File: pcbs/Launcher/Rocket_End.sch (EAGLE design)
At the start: 28 parts, among them IC1 7805TV, K4 LD105, K5 LD105, K6 LD105, K7 LD105, T1 BC547, T2 BC547, T3 BC547, T4 BC547, T5 BC547, U1 ARDUINO-MEGAPRO-5V, X1 22-23-2041, X2 22-23-2041, X4 22-23-2021, X5 22-23-2021, X6 22-23-2021

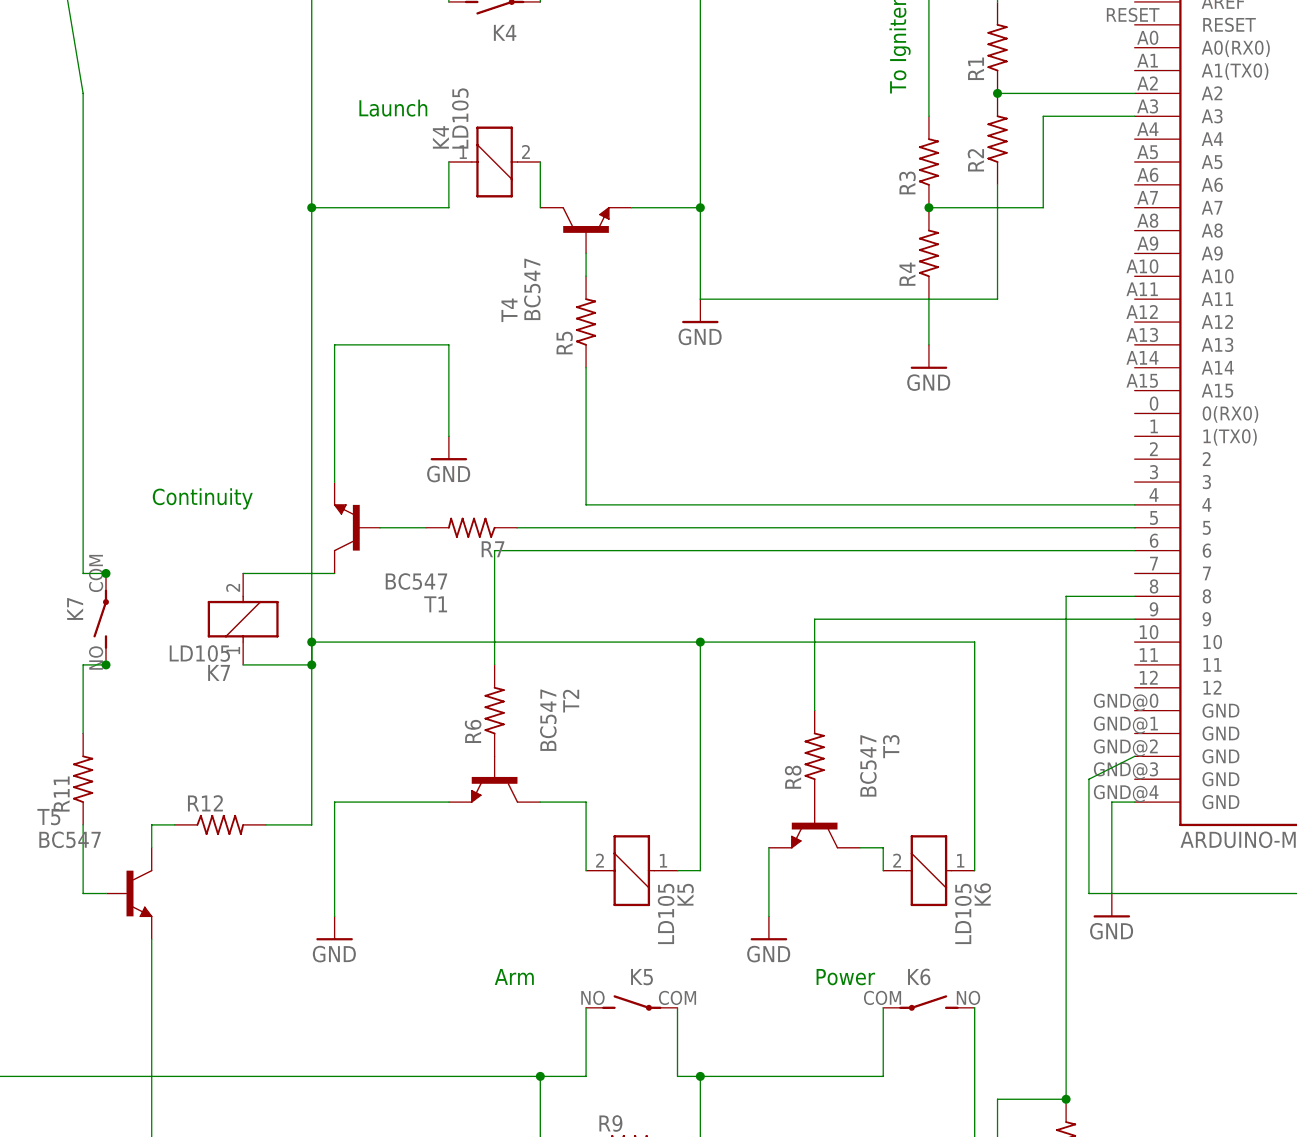
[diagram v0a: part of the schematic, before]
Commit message: * Much better placement of components and tracks for Rocket_End * Put IMU on bottom of the Sensor board
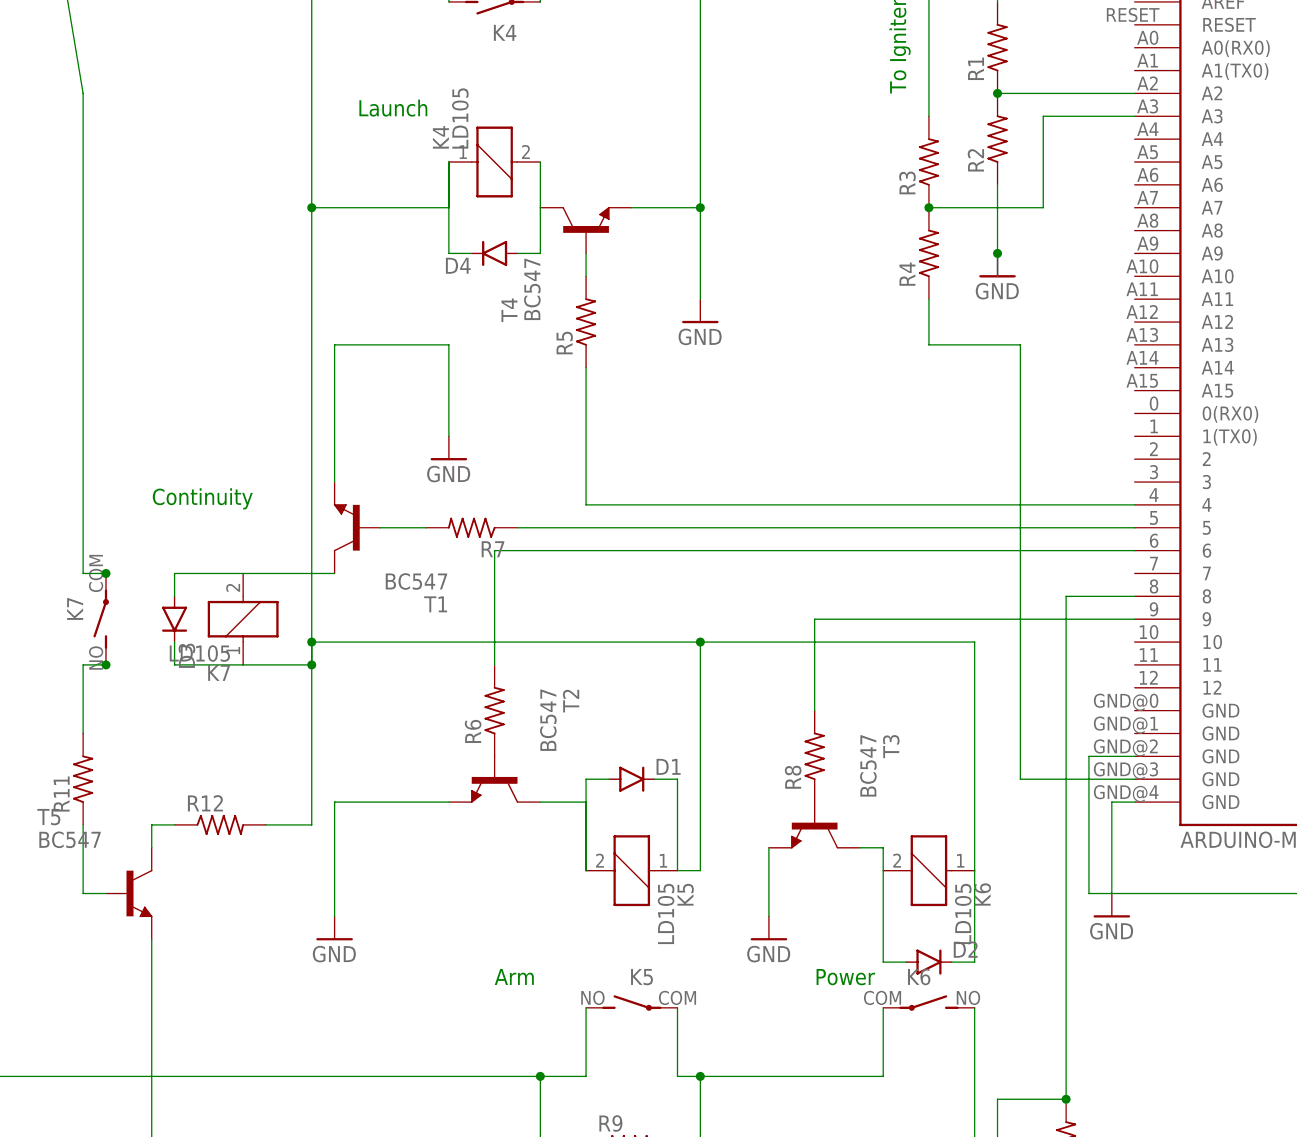
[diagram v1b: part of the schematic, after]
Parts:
- added D1, D2, D3, D4: (no value), SparkFun-DiscreteSemi:DIODE1N4148
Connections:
- new net N$24: R4.1, U1.GND@3
- net GND: no longer R4.1
- net N$19: now also D4.A
- net N$20: now also D3.A
- net N$21: now also D2.A
- net N$22: now also D1.A
- net N$5: now also D1.C, D2.C, D3.C, D4.C
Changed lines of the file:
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@@
 <?xml version="1.0" encoding="utf-8"?>
 <!DOCTYPE eagle SYSTEM "eagle.dtd">
-<eagle version="7.3.0">
+<eagle version="7.1.0">
 <drawing>
 <settings>
@@
 <layer number="223" name="223bmp" color="24" fill="1" visible="no" active="no"/>
 <layer number="224" name="224bmp" color="25" fill="1" visible="no" active="no"/>
+<layer number="225" name="225bmp" color="7" fill="1" visible="yes" active="yes"/>
+<layer number="226" name="226bmp" color="7" fill="1" visible="yes" active="yes"/>
+<layer number="227" name="227bmp" color="7" fill="1" visible="yes" active="yes"/>
+<layer number="228" name="228bmp" color="7" fill="1" visible="yes" active="yes"/>
+<layer number="229" name="229bmp" color="7" fill="1" visible="yes" active="yes"/>
+<layer number="230" name="230bmp" color="7" fill="1" visible="yes" active="yes"/>
+<layer number="231" name="231bmp" color="7" fill="1" visible="yes" active="yes"/>
 <layer number="248" name="Housing" color="7" fill="1" visible="yes" active="yes"/>
 <layer number="249" name="Edge" color="7" fill="1" visible="yes" active="yes"/>
@@
 <part name="R3" library="rcl" deviceset="R-US_" device="0204/7"/>
 <part name="R4" library="rcl" deviceset="R-US_" device="0204/7"/>
-<part name="GND2" library="supply1" deviceset="GND" device=""/>
 <part name="SUPPLY1" library="supply2" deviceset="VCC" device=""/>
 <part name="R5" library="resistor" deviceset="R-US_" device="0204/7"/>
@@
 <part name="K6" library="relay" deviceset="LD?*" device="1" technology="05"/>
 <part name="K7" library="relay" deviceset="LD?*" device="1" technology="05"/>
+<part name="D1" library="SparkFun-DiscreteSemi" deviceset="DIODE" device="1N4148"/>
+<part name="D2" library="SparkFun-DiscreteSemi" deviceset="DIODE" device="1N4148"/>
+<part name="D3" library="SparkFun-DiscreteSemi" deviceset="DIODE" device="1N4148"/>
+<part name="D4" library="SparkFun-DiscreteSemi" deviceset="DIODE" device="1N4148"/>
+<part name="GND1" library="supply1" deviceset="GND" device=""/>
 </parts>
 <sheets>
@@
 <instance part="R3" gate="G$1" x="-5.08" y="73.66" rot="R90"/>
 <instance part="R4" gate="G$1" x="-5.08" y="63.5" rot="R90"/>
-<instance part="GND2" gate="1" x="-5.08" y="50.8"/>
 <instance part="SUPPLY1" gate="G$1" x="2.54" y="116.84"/>
 <instance part="R5" gate="G$1" x="-43.18" y="55.88" rot="R90"/>
@@
 <instance part="K7" gate="1" x="-81.28" y="22.86" rot="R180"/>
 <instance part="K7" gate="2" x="-96.52" y="22.86" rot="MR180"/>
+<instance part="D1" gate="G$1" x="-38.1" y="5.08"/>
+<instance part="D2" gate="G$1" x="-5.08" y="-15.24"/>
+<instance part="D3" gate="G$1" x="-88.9" y="22.86" rot="R270"/>
+<instance part="D4" gate="G$1" x="-53.34" y="63.5" rot="R180"/>
+<instance part="GND1" gate="1" x="2.54" y="60.96"/>
 </instances>
 <busses>
@@
 <net name="GND" class="0">
 <segment>
-<pinref part="R4" gate="G$1" pin="1"/>
-<pinref part="R2" gate="G$1" pin="1"/>
-<wire x1="-5.08" y1="58.42" x2="-5.08" y2="53.34" width="0.1524" layer="91"/>
-<wire x1="2.54" y1="71.12" x2="2.54" y2="58.42" width="0.1524" layer="91"/>
-<wire x1="2.54" y1="58.42" x2="-5.08" y2="58.42" width="0.1524" layer="91"/>
-<pinref part="GND2" gate="1" pin="GND"/>
 <pinref part="T4" gate="G$1" pin="E"/>
 <wire x1="-38.1" y1="68.58" x2="-30.48" y2="68.58" width="0.1524" layer="91"/>
@@
 <junction x="-30.48" y="68.58"/>
 <pinref part="K4" gate="2" pin="P"/>
-<wire x1="-5.08" y1="58.42" x2="-30.48" y2="58.42" width="0.1524" layer="91"/>
 </segment>
 <segment>
@@
 <junction x="-101.6" y="132.08"/>
 </segment>
+<segment>
+<pinref part="R2" gate="G$1" pin="1"/>
+<wire x1="2.54" y1="71.12" x2="2.54" y2="63.5" width="0.1524" layer="91"/>
+<pinref part="GND1" gate="1" pin="GND"/>
+<wire x1="2.54" y1="63.5" x2="2.54" y2="60.96" width="0.1524" layer="91"/>
+<junction x="2.54" y="63.5"/>
+</segment>
 </net>
 <net name="VCC" class="0">
@@
 <wire x1="-48.26" y1="68.58" x2="-48.26" y2="73.66" width="0.1524" layer="91"/>
 <pinref part="K4" gate="1" pin="2"/>
+<pinref part="D4" gate="G$1" pin="A"/>
+<wire x1="-50.8" y1="63.5" x2="-48.26" y2="63.5" width="0.1524" layer="91"/>
+<wire x1="-48.26" y1="63.5" x2="-48.26" y2="68.58" width="0.1524" layer="91"/>
 </segment>
 </net>
@@
 <wire x1="-71.12" y1="27.94" x2="-81.28" y2="27.94" width="0.1524" layer="91"/>
 <pinref part="K7" gate="1" pin="2"/>
+<pinref part="D3" gate="G$1" pin="A"/>
+<wire x1="-88.9" y1="25.4" x2="-88.9" y2="27.94" width="0.1524" layer="91"/>
+<wire x1="-81.28" y1="27.94" x2="-88.9" y2="27.94" width="0.1524" layer="91"/>
 </segment>
 </net>
@@
 <wire x1="-10.16" y1="-2.54" x2="-10.16" y2="-5.08" width="0.1524" layer="91"/>
 <pinref part="K6" gate="1" pin="2"/>
+<pinref part="D2" gate="G$1" pin="A"/>
+<wire x1="-7.62" y1="-15.24" x2="-10.16" y2="-15.24" width="0.1524" layer="91"/>
+<wire x1="-10.16" y1="-15.24" x2="-10.16" y2="-5.08" width="0.1524" layer="91"/>
 </segment>
 </net>
@@
 <wire x1="-43.18" y1="2.54" x2="-43.18" y2="-5.08" width="0.1524" layer="91"/>
 <pinref part="K5" gate="1" pin="2"/>
+<wire x1="-43.18" y1="-5.08" x2="-43.18" y2="5.08" width="0.1524" layer="91"/>
+<pinref part="D1" gate="G$1" pin="A"/>
+<wire x1="-43.18" y1="5.08" x2="-40.64" y2="5.08" width="0.1524" layer="91"/>
 </segment>
 </net>
@@
 <junction x="-73.66" y="20.32"/>
 <junction x="-73.66" y="17.78"/>
-<wire x1="-30.48" y1="-5.08" x2="-30.48" y2="20.32" width="0.1524" layer="91"/>
 <junction x="-30.48" y="20.32"/>
 <pinref part="IC1" gate="A1" pin="VO"/>
+<wire x1="-30.48" y1="-5.08" x2="-30.48" y2="20.32" width="0.1524" layer="91"/>
 <wire x1="-73.66" y1="139.7" x2="-76.2" y2="139.7" width="0.1524" layer="91"/>
 <junction x="-73.66" y="132.08"/>
@@
 <wire x1="-33.02" y1="-5.08" x2="-30.48" y2="-5.08" width="0.1524" layer="91"/>
 <pinref part="K6" gate="1" pin="1"/>
+<wire x1="-81.28" y1="17.78" x2="-88.9" y2="17.78" width="0.1524" layer="91"/>
+<pinref part="D3" gate="G$1" pin="C"/>
+<wire x1="-88.9" y1="17.78" x2="-88.9" y2="20.32" width="0.1524" layer="91"/>
+<wire x1="-33.02" y1="-5.08" x2="-33.02" y2="5.08" width="0.1524" layer="91"/>
+<pinref part="D1" gate="G$1" pin="C"/>
+<wire x1="-33.02" y1="5.08" x2="-35.56" y2="5.08" width="0.1524" layer="91"/>
+<pinref part="D4" gate="G$1" pin="C"/>
+<wire x1="-55.88" y1="63.5" x2="-58.42" y2="63.5" width="0.1524" layer="91"/>
+<wire x1="-58.42" y1="63.5" x2="-58.42" y2="73.66" width="0.1524" layer="91"/>
+<wire x1="0" y1="-5.08" x2="0" y2="-15.24" width="0.1524" layer="91"/>
+<pinref part="D2" gate="G$1" pin="C"/>
+<wire x1="0" y1="-15.24" x2="-2.54" y2="-15.24" width="0.1524" layer="91"/>
 </segment>
 </net>
@@
 <wire x1="86.36" y1="83.82" x2="86.36" y2="-7.62" width="0.1524" layer="91"/>
 <wire x1="86.36" y1="-7.62" x2="12.7" y2="-7.62" width="0.1524" layer="91"/>
-<wire x1="12.7" y1="-7.62" x2="12.7" y2="5.08" width="0.1524" layer="91"/>
-<wire x1="12.7" y1="5.08" x2="17.78" y2="7.62" width="0.1524" layer="91"/>
+<wire x1="12.7" y1="-7.62" x2="12.7" y2="7.62" width="0.1524" layer="91"/>
+<wire x1="12.7" y1="7.62" x2="17.78" y2="7.62" width="0.1524" layer="91"/>
 <pinref part="U1" gate="G$1" pin="GND@2"/>
 </segment>
 </net>
+<net name="N$24" class="0">
+<segment>
+<pinref part="R4" gate="G$1" pin="1"/>
+<wire x1="-5.08" y1="58.42" x2="-5.08" y2="53.34" width="0.1524" layer="91"/>
+<wire x1="-5.08" y1="53.34" x2="5.08" y2="53.34" width="0.1524" layer="91"/>
+<wire x1="5.08" y1="53.34" x2="5.08" y2="5.08" width="0.1524" layer="91"/>
+<pinref part="U1" gate="G$1" pin="GND@3"/>
+<wire x1="5.08" y1="5.08" x2="17.78" y2="5.08" width="0.1524" layer="91"/>
+</segment>
+</net>
